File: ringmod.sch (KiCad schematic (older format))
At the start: 12 parts, among them T1 audio_transformer, T2 audio_transformer

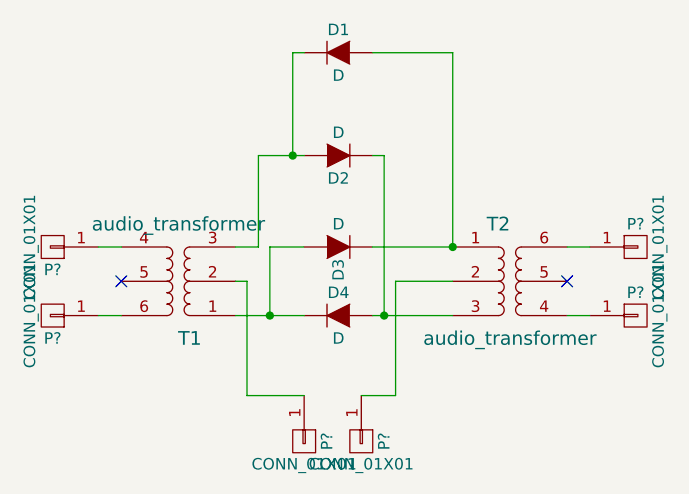
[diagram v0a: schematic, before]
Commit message: fix schematic and enlarge mechanical holes for the transformers
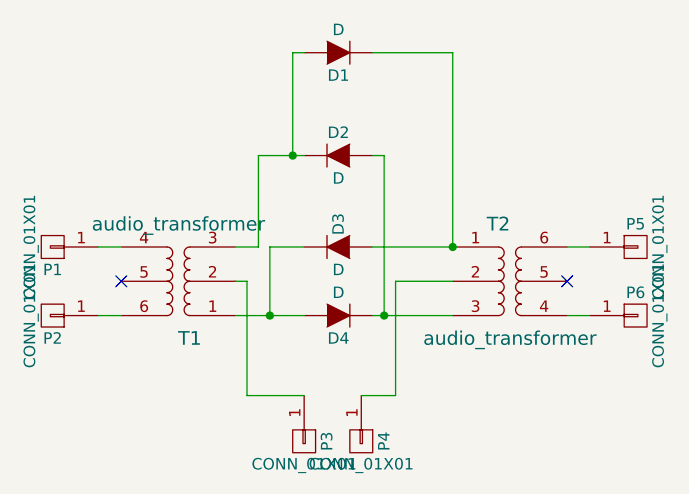
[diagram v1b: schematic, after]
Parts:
- P1, P2, P3, P4, P5, P6: renamed from P?; footprint (none) -> Wire_Pads:SolderWirePad_single_1-2mmDrill
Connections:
- new net: D1.1 (K), D3.2 (A), T2.1
- new net: D1.2 (A), D2.1 (K), T1.3
- new net: D2.2 (A), D4.1 (K), T2.3
- new net: D3.1 (K), D4.2 (A), T1.1
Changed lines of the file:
@@
 LIBS:valves
 LIBS:audio_transformer
+LIBS:ringmod-cache
 EELAYER 25 0
 EELAYER END
@@
 F 3 "" H 4900 2500 50  0000 C CNN
 	1    4900 2500
-	1    0    0    -1
+	-1   0    0    1
 $EndComp
 $Comp
@@
 F 3 "" H 4900 2950 50  0000 C CNN
 	1    4900 2950
-	-1   0    0    1
+	1    0    0    -1
 $EndComp
 $Comp
@@
 F 3 "" H 4900 3350 50  0000 C CNN
 	1    4900 3350
-	-1   0    0    1
+	1    0    0    -1
 $EndComp
 $Comp
@@
 F 3 "" H 4900 3650 50  0000 C CNN
 	1    4900 3650
-	1    0    0    -1
+	-1   0    0    1
 $EndComp
 $Comp
@@
 	3950 3650 3850 3650
 $Comp
-L CONN_01X01 P?
+L CONN_01X01 P5
 U 1 1 573C67E5
 P 6200 3350
-F 0 "P?" H 6200 3450 50  0000 C CNN
+F 0 "P5" H 6200 3450 50  0000 C CNN
 F 1 "CONN_01X01" V 6300 3350 50  0000 C CNN
-F 2 "" H 6200 3350 50  0000 C CNN
+F 2 "Wire_Pads:SolderWirePad_single_1-2mmDrill" H 6200 3350 50  0001 C CNN
 F 3 "" H 6200 3350 50  0000 C CNN
 	1    6200 3350
@@
 $EndComp
 $Comp
-L CONN_01X01 P?
+L CONN_01X01 P6
 U 1 1 573C68C8
 P 6200 3650
-F 0 "P?" H 6200 3750 50  0000 C CNN
+F 0 "P6" H 6200 3750 50  0000 C CNN
 F 1 "CONN_01X01" V 6300 3650 50  0000 C CNN
-F 2 "" H 6200 3650 50  0000 C CNN
+F 2 "Wire_Pads:SolderWirePad_single_1-2mmDrill" H 6200 3650 50  0001 C CNN
 F 3 "" H 6200 3650 50  0000 C CNN
 	1    6200 3650
@@
 $EndComp
 $Comp
-L CONN_01X01 P?
+L CONN_01X01 P1
 U 1 1 573C695F
 P 3650 3350
-F 0 "P?" H 3650 3450 50  0000 C CNN
+F 0 "P1" H 3650 3450 50  0000 C CNN
 F 1 "CONN_01X01" V 3750 3350 50  0000 C CNN
-F 2 "" H 3650 3350 50  0000 C CNN
+F 2 "Wire_Pads:SolderWirePad_single_1-2mmDrill" H 3650 3350 50  0001 C CNN
 F 3 "" H 3650 3350 50  0000 C CNN
 	1    3650 3350
@@
 $EndComp
 $Comp
-L CONN_01X01 P?
+L CONN_01X01 P2
 U 1 1 573C6A45
 P 3650 3650
-F 0 "P?" H 3650 3750 50  0000 C CNN
+F 0 "P2" H 3650 3750 50  0000 C CNN
 F 1 "CONN_01X01" V 3750 3650 50  0000 C CNN
-F 2 "" H 3650 3650 50  0000 C CNN
+F 2 "Wire_Pads:SolderWirePad_single_1-2mmDrill" H 3650 3650 50  0001 C CNN
 F 3 "" H 3650 3650 50  0000 C CNN
 	1    3650 3650
@@
 $EndComp
 $Comp
-L CONN_01X01 P?
+L CONN_01X01 P4
 U 1 1 573C6C20
 P 5000 4200
-F 0 "P?" H 5000 4300 50  0000 C CNN
+F 0 "P4" H 5000 4300 50  0000 C CNN
 F 1 "CONN_01X01" V 5100 4200 50  0000 C CNN
-F 2 "" H 5000 4200 50  0000 C CNN
+F 2 "Wire_Pads:SolderWirePad_single_1-2mmDrill" H 5000 4200 50  0001 C CNN
 F 3 "" H 5000 4200 50  0000 C CNN
 	1    5000 4200
@@
 $EndComp
 $Comp
-L CONN_01X01 P?
+L CONN_01X01 P3
 U 1 1 573C6CB3
 P 4750 4200
-F 0 "P?" H 4750 4300 50  0000 C CNN
+F 0 "P3" H 4750 4300 50  0000 C CNN
 F 1 "CONN_01X01" V 4850 4200 50  0000 C CNN
-F 2 "" H 4750 4200 50  0000 C CNN
+F 2 "Wire_Pads:SolderWirePad_single_1-2mmDrill" H 4750 4200 50  0001 C CNN
 F 3 "" H 4750 4200 50  0000 C CNN
 	1    4750 4200
